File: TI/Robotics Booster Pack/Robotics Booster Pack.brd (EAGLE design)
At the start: 68.6 x 76.2 mm, 116 parts, among them J1 1X2.PTS, U1 TS3A44159.RGT, U10 74LVTH125.RGY, U11 SCHA4B0400, U12 BLUETOOTH-RN41", U13 XBEE-1XBEE-1_LOCK, U14 TPS5450, U15 TPS715XX.DCK, U16 TPS6215X.RGT, U3 DRV8800, U4 DRV8800, U5 DRV8800, U6 DRV8800, U7 PCA9557.RGV, U8 MPU-6050, U9 INA220.DGS

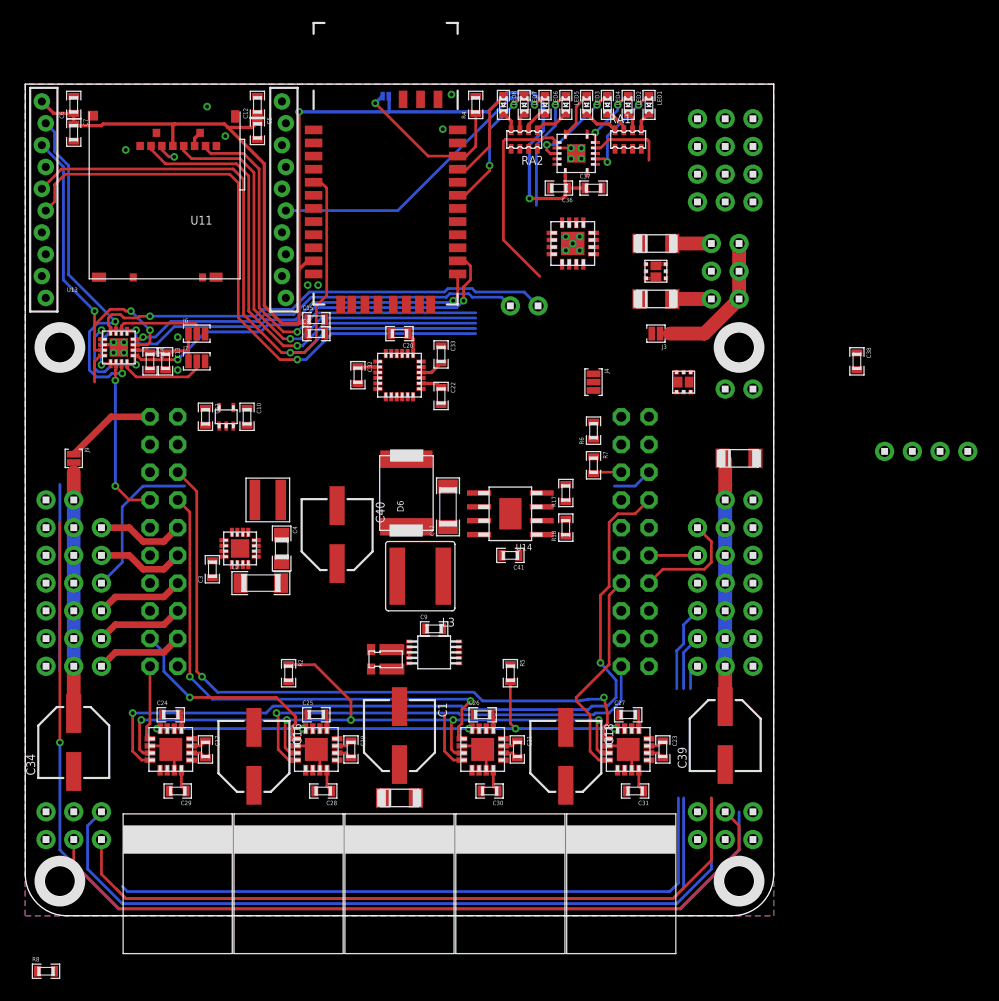
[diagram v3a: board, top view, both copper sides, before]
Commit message: More Robotics BP v2 routing. Power regulators routed and completed Most IO Expander signals completely routed
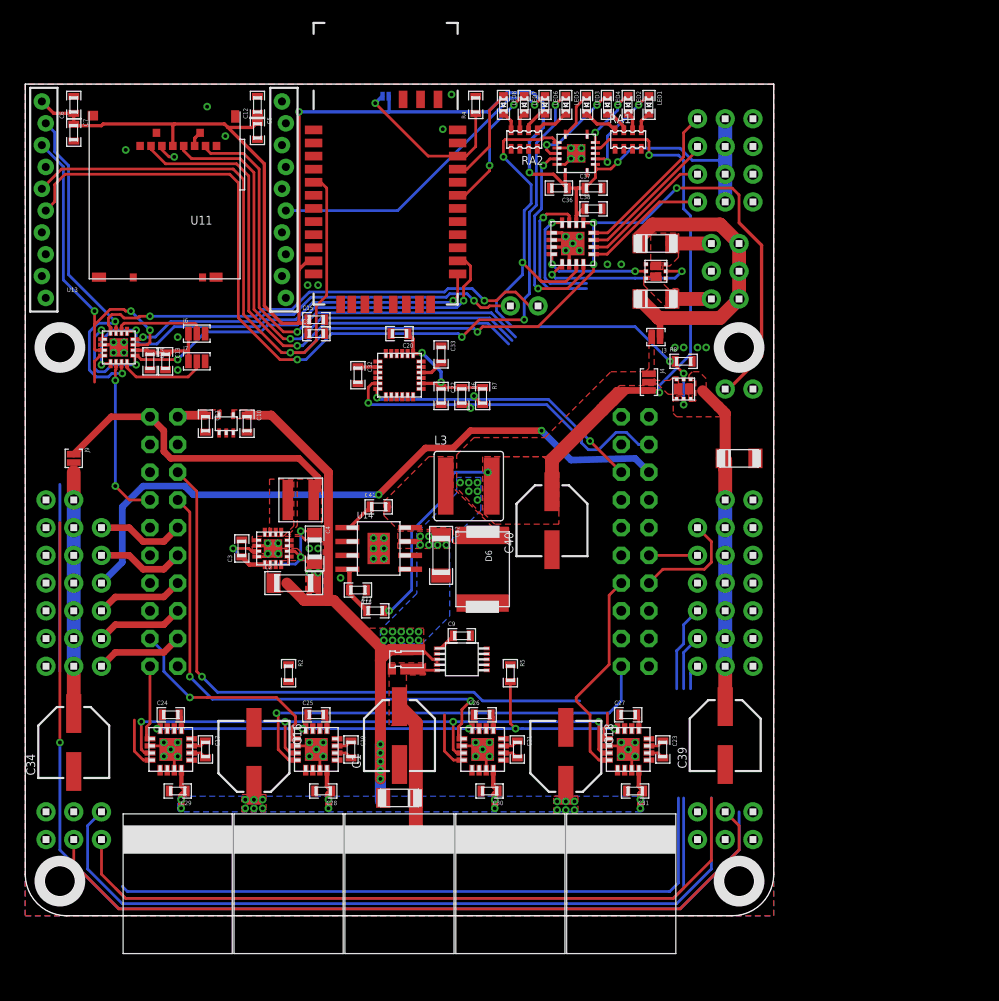
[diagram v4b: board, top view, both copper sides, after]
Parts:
- removed U$6: 1X4, headers(.1in):1X4
- U16: value TPS6215X.RGT -> TPS62152.RGT
- moved R8 80.8 mm to (60.3, 50.8)
- moved C38 27.9 mm to (52.1, 64.8), turned to 0 degrees
- moved R17 20.5 mm to (32.1, 27.9), turned to 0 degrees
- moved R18 19.9 mm to (30.5, 29.8), turned to 180 degrees
- moved C40 19.7 mm to (48.3, 36.2), turned to 90 degrees
- moved C41 12.9 mm to (32.4, 37.5), turned to 0 degrees
- moved U14 12.5 mm to (32.4, 33.7), turned to 0 degrees
- moved R6 12.5 mm to (40.0, 47.6), turned to 270 degrees
- moved R7 12.0 mm to (41.9, 47.6)
- moved D6 9.88 mm to (41.9, 31.8), turned to 270 degrees
- moved L3 9.38 mm to (40.6, 39.4), turned to 0 degrees
- moved J4 5.08 mm to (57.1, 48.9)
- moved C42 4.49 mm to (38.1, 33.0), turned to 270 degrees
- moved C3 3.30 mm to (19.8, 33.7)
- moved U16 3.02 mm to (22.7, 33.7)
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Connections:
- removed net SVRO.EN: Q2.2, Q2.5, R8.1
- net 3.3V: no longer U$6.1
- net GND: now also C1.-; no longer U$6.4
- net I2C.SCL: no longer U$6.3
- net I2C.SDA: no longer U$6.2
- net SRVO.EN: now also Q2.2, Q2.5, R8.1
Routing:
- net 3.3V: track 202.2 -> 271.0 mm, vias 2 -> 8
- net M0.DIR: track 72.0 -> 4.63 mm, vias 2 -> 0
- net VBAT: track 8.86 -> 75.3 mm, vias 0 -> 47
- net 5.0V: track 7.04 -> 72.8 mm, vias 0 -> 4
- net !RST: track 74.3 -> 128.0 mm, vias 1 -> 5
- net I2C.SCL: track 0.00 -> 46.3 mm, vias 0 -> 3
- net AD2: track 18.0 -> 61.2 mm, vias 0 -> 2
- net I2C.SDA: track 2.60 -> 37.9 mm, vias 0 -> 4
- net SRVO.EN: track 19.0 -> 53.6 mm, vias 0 -> 5
- net VFET: track 12.7 -> 30.8 mm
- net XBEE.RSSI: track 68.2 -> 84.3 mm, vias 2 -> 4
- net N$22: track 0.00 -> 15.5 mm
- net IO0: track 0.00 -> 15.2 mm
- net FET1.G: track 0.00 -> 15.1 mm, vias 0 -> 2
- net IO1: track 0.00 -> 13.3 mm
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- added copper zone on layer 1, net 3.3V
- added copper zone on layer 1, net 5.0V
- added copper zone on layer 1, net N$1
- added copper zone on layer 1, net N$16
- added copper zone on layer 1, net N$22
- added copper zone on layer 1, net N$34
- added copper zone on layer 1, net VBAT
- added copper zone on layer 16, net VBAT
- added copper zone on layer 1, net VBUS
- added copper zone on layer 1, net VSERVO
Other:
- board text added: "5V"
- board text added: "VSVRO"
- board text removed: "I2C"
- board text removed: "SCL"
- board text removed: "SDA"

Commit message: More Routing for Robotics Booster Pack v2. Assuming UART0 header is oriented correctly, the top 25% of board is completely routed!
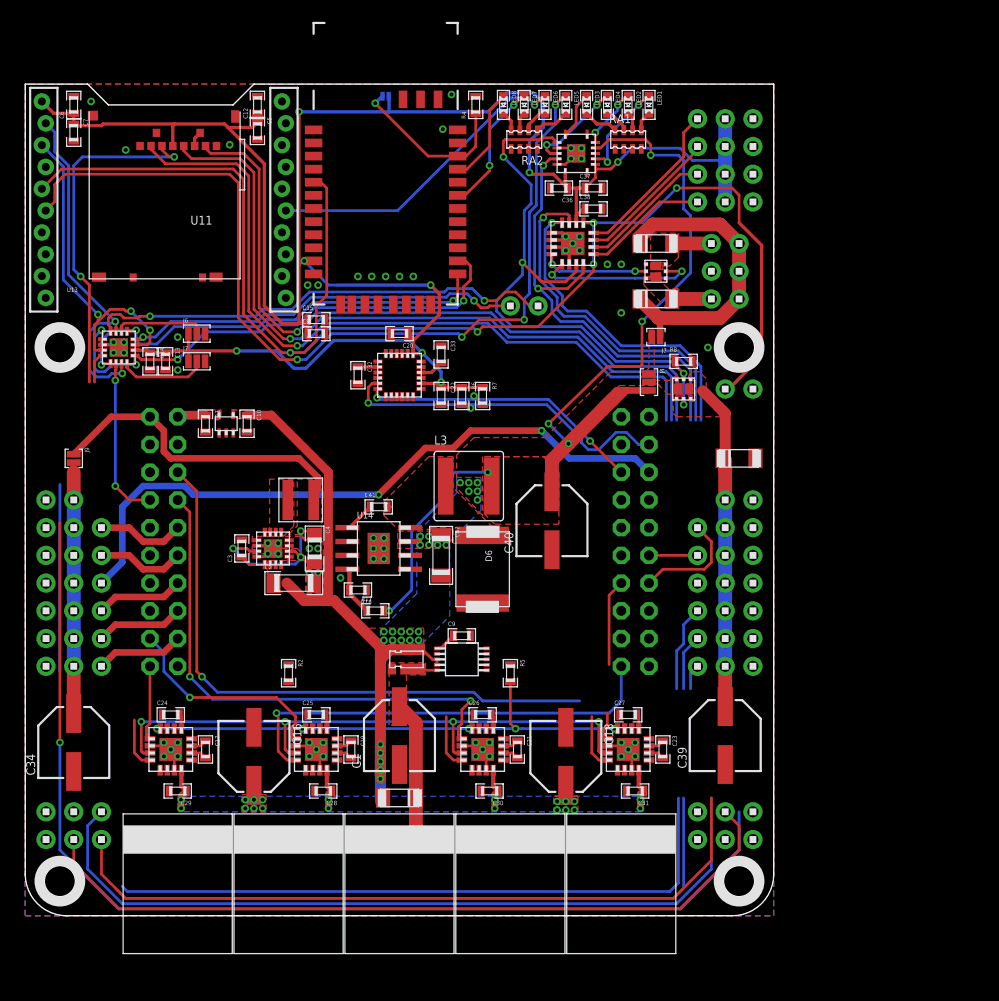
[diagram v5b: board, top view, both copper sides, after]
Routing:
- net 3.3V: track 271.0 -> 313.3 mm, vias 8 -> 11
- net SPI.MOSI: track 1.75 -> 31.7 mm, vias 1 -> 2
- net M.EN: track 91.8 -> 114.5 mm
- net SPI.MISO: track 44.7 -> 65.0 mm
- net SPI.SCLK: track 46.7 -> 66.6 mm
- net SPI.!CS: track 49.4 -> 68.9 mm
- net I2C.SDA: track 37.9 -> 57.0 mm
- net I2C.SCL: track 46.3 -> 64.8 mm
- net 5.0V: track 72.8 -> 83.0 mm, vias 4 -> 6
- net M3.DIR: track 19.6 -> 13.0 mm
- net SRVO.EN: track 53.6 -> 54.7 mm, vias 5 -> 4
- net GND: vias 63 -> 66
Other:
- outline, holes or cut-outs redrawn

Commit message: Even more routing! With any luck, all routing will be completed by the end of tomorrow ^^;
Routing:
- net SVRO4: track 66.2 -> 111.6 mm
- net SVRO5: track 61.6 -> 103.6 mm
- net QEI1.B: track 0.00 -> 29.3 mm
- net SPI.MOSI: track 31.7 -> 57.7 mm, vias 2 -> 5
- net SVRO3: track 108.1 -> 132.1 mm
- net SPI.SCLK: track 66.6 -> 90.0 mm
- net QEI1.A: track 0.00 -> 23.2 mm, vias 0 -> 1
- net SPI.!CS: track 68.9 -> 89.6 mm
- net SPI.MISO: track 65.0 -> 85.3 mm, vias 1 -> 3
- net !RST: track 128.0 -> 144.7 mm, vias 5 -> 6
- net I2C.SCL: track 64.8 -> 77.2 mm, vias 3 -> 5
- net 3.3V: track 313.3 -> 323.8 mm
- net UART1.RXI: track 2.87 -> 13.2 mm, vias 0 -> 1
- net QEI0.B: track 72.1 -> 82.2 mm
- net M0.DIR: track 4.72 -> 10.2 mm
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
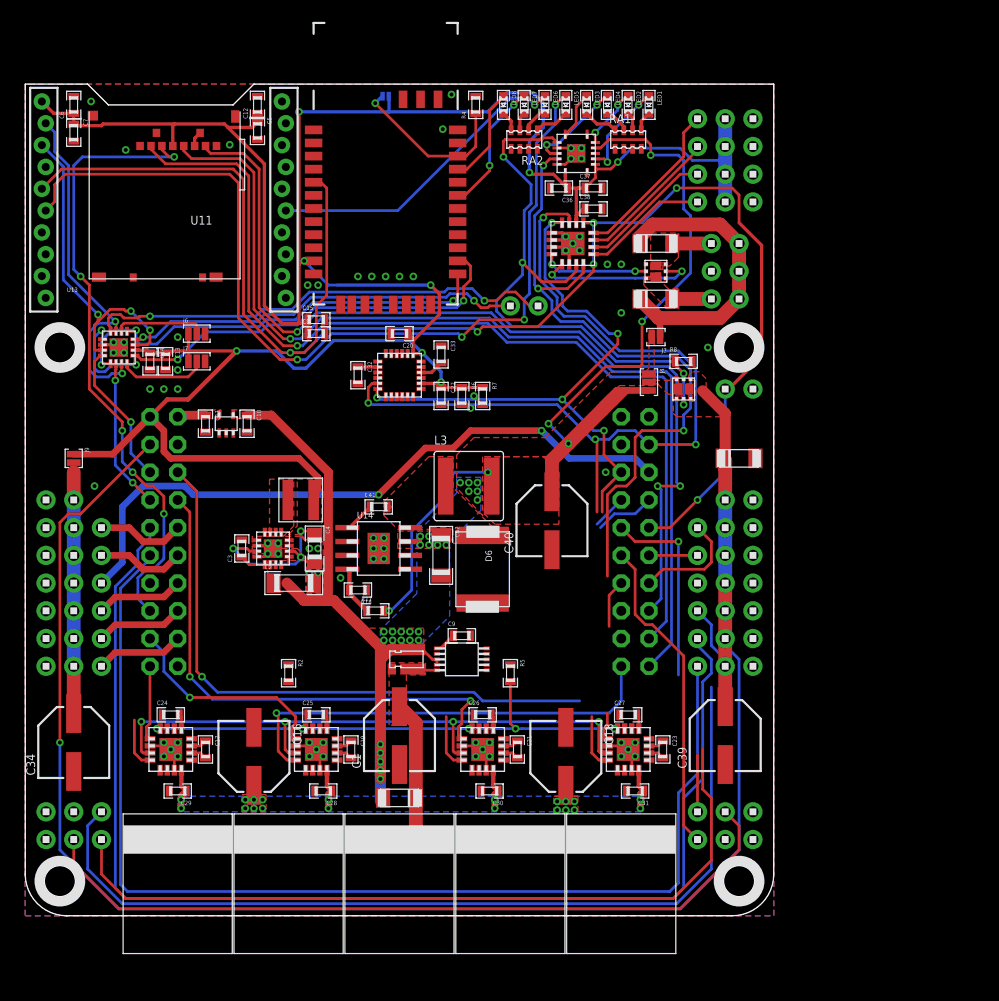
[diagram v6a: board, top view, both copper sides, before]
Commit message: Robotics BoosterPack v2 Complete! Still need to double check a few mote things, and clean up the silkscreen.
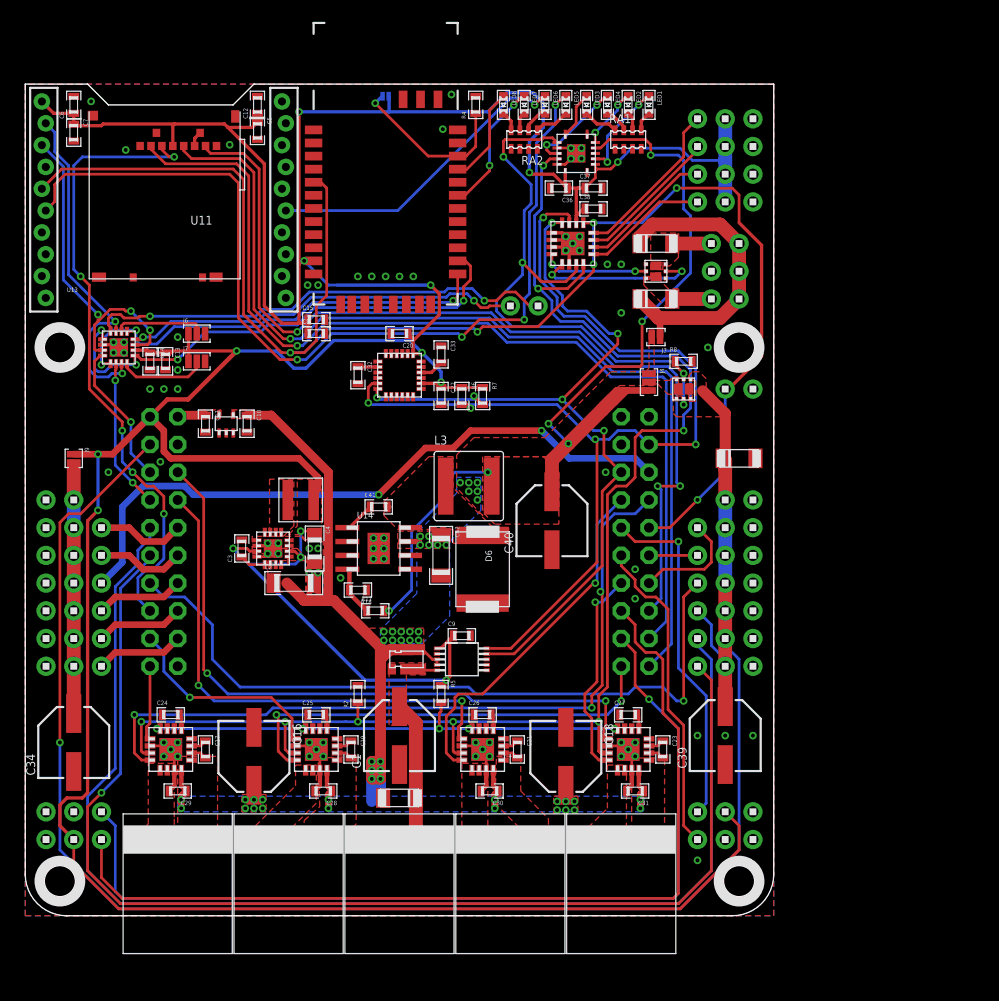
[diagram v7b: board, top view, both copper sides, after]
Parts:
- L3: value (none) -> 10uH
- R18: value 2.87k -> 3.24k
- moved R2 6.63 mm to (30.5, 20.3), turned to 90 degrees
- moved R5 6.63 mm to (38.1, 20.3)
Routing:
- net SVRO2: track 0.00 -> 67.1 mm, vias 0 -> 1
- net 3.3V: track 323.8 -> 388.9 mm, vias 11 -> 14
- net M0.DIR: track 10.2 -> 69.8 mm, vias 0 -> 3
- net M2.DIR: track 8.18 -> 32.9 mm, vias 0 -> 1
- net I2C.SDA: track 57.0 -> 75.9 mm
- net I2C.SCL: track 77.2 -> 95.1 mm
- net M.EN: track 117.6 -> 133.0 mm, vias 7 -> 8
- net QEI0.A: track 71.9 -> 85.9 mm
- net M3.DIR: track 9.47 -> 19.4 mm, vias 0 -> 1
- net QEI1.A: track 23.2 -> 31.9 mm
- net GND: track 32.0 -> 40.4 mm, vias 71 -> 78
- net SVRO5: track 103.6 -> 110.2 mm, vias 0 -> 1
- net VBAT: track 75.3 -> 81.3 mm, vias 47 -> 48
- net SVRO4: track 111.6 -> 115.2 mm
- net QEI0.B: track 82.2 -> 85.4 mm, vias 0 -> 1
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- added copper zone on layer 1, net M0+
- added copper zone on layer 1, net M0-
- added copper zone on layer 1, net M1+
- added copper zone on layer 1, net M1-
- added copper zone on layer 1, net M2+
- added copper zone on layer 1, net M2-
- added copper zone on layer 1, net M3-
- added copper zone on layer 1, net N$4

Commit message: Cleaned up completed Robotics Booster Pack v2. Sent off to OSHPark!
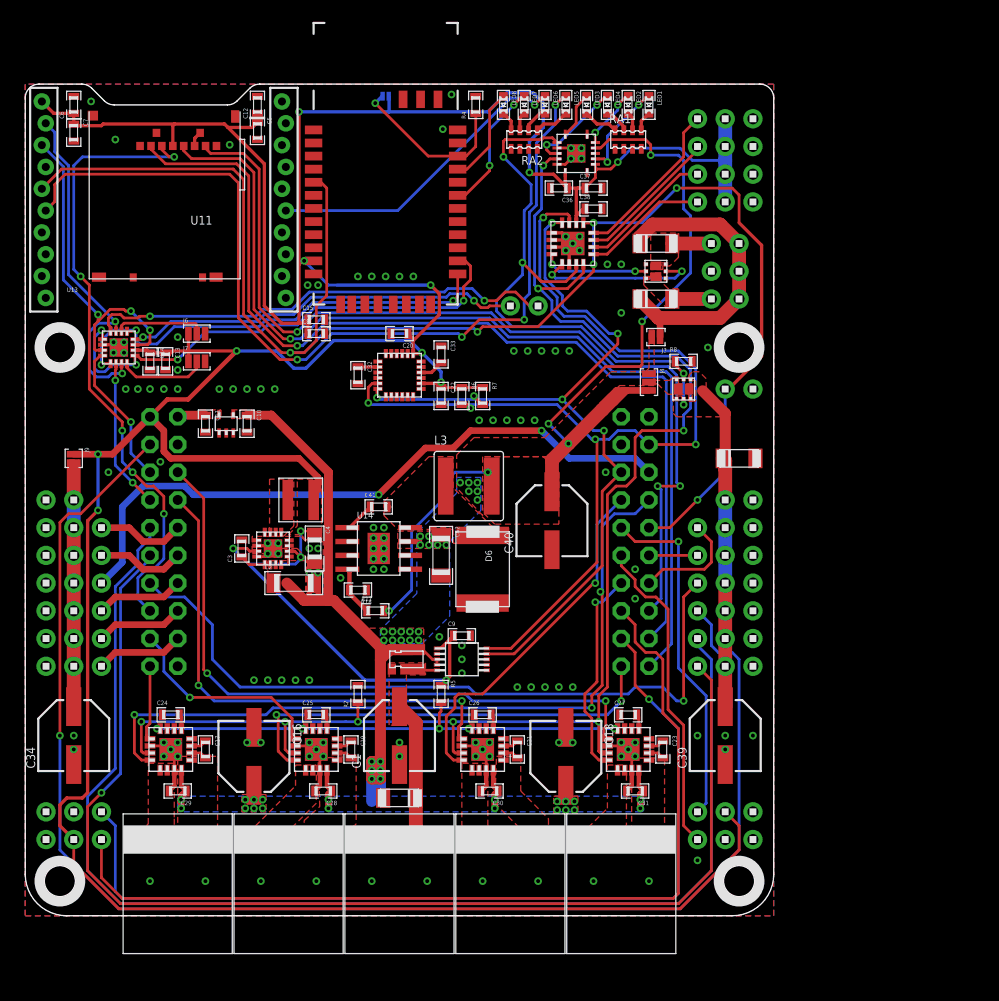
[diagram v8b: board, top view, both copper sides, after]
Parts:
- J4: device solderjumper:3.LRG.12 -> solderjumper:3.LRG.23
- moved C34 0.64 mm to (4.45, 16.5)
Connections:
- net M0+: now also H17.1, U5.9; no longer H17.2, U5.6
- net M0-: now also H17.2, U5.6; no longer H17.1, U5.9
- net M1+: now also H18.1, U6.9; no longer H18.2, U6.6
- net M1-: now also H18.2, U6.6; no longer H18.1, U6.9
- net M2+: now also H19.1, U3.9; no longer H19.2, U3.6
- net M2-: now also H19.2, U3.6; no longer H19.1, U3.9
- net M3+: now also H20.1, U4.9; no longer H20.2, U4.6
- net M3-: now also H20.2, U4.6; no longer H20.1, U4.9
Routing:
- net N$4: track 22.6 -> 22.0 mm
- net GND: vias 78 -> 132
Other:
- outline, holes or cut-outs redrawn
- board text added: "VSRVO"
